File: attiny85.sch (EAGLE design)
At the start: 9 parts, among them U2 ATTINY85V-10SU

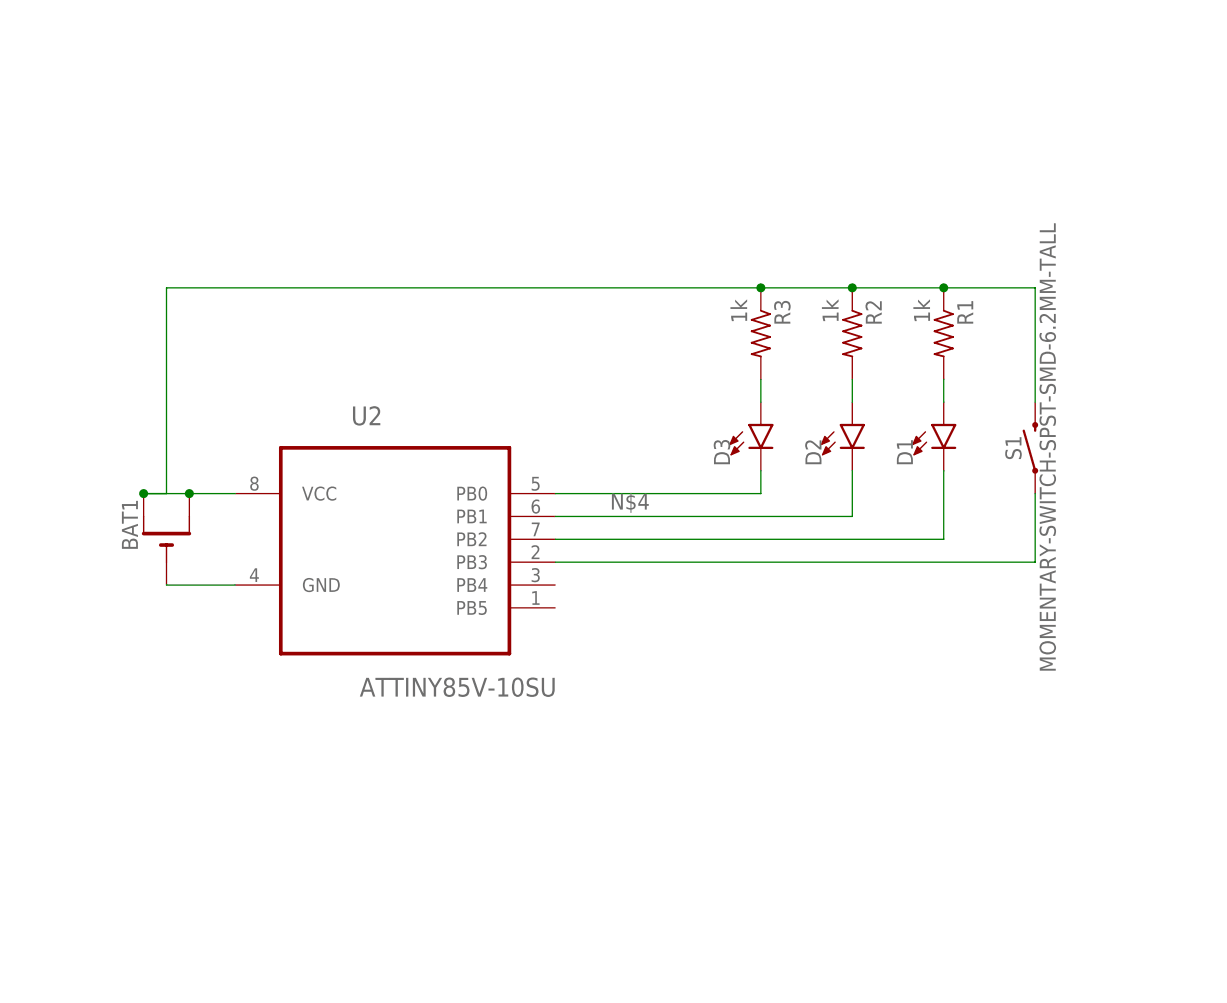
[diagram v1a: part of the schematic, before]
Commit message: Flipping to output through the attiny
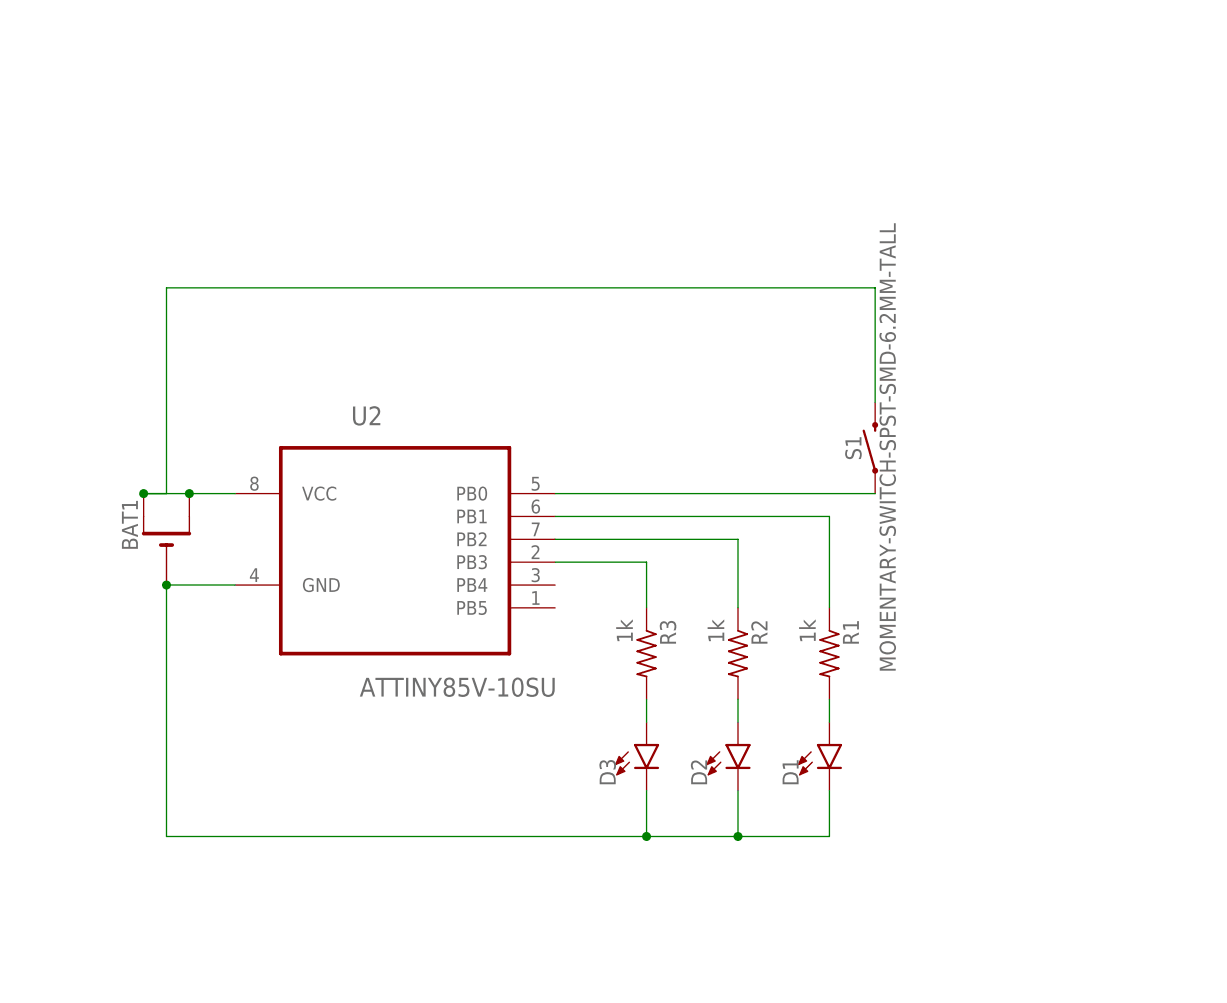
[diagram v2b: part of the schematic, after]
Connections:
- removed net VCC: BAT1.+, BAT1.+1, R1.1, R2.1, R3.1, S1.2, U2.VCC
- new net N$8: R3.1, U2.PB3
- net GND: now also D1.C, D2.C, D3.C
- net N$3: now also BAT1.+, BAT1.+1, S1.2, U2.VCC; no longer D3.C, U2.PB0
- net N$4: now also R1.1; no longer D2.C
- net N$6: now also S1.1, U2.PB0; no longer D1.C, U2.PB2
- net N$7: now also R2.1, U2.PB2; no longer S1.1, U2.PB3
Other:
- moved on the sheet: D1, D2, D3, R1, R2, R3, S1
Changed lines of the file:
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@@
 <instance part="FRAME1" gate="G$1" x="0" y="0"/>
 <instance part="FRAME1" gate="G$2" x="299.72" y="0"/>
-<instance part="R2" gate="G$1" x="106.68" y="220.98" rot="R270"/>
-<instance part="D2" gate="G$1" x="106.68" y="210.82"/>
-<instance part="R3" gate="G$1" x="96.52" y="220.98" rot="R270"/>
-<instance part="D3" gate="G$1" x="96.52" y="210.82"/>
+<instance part="R2" gate="G$1" x="93.98" y="185.42" rot="R270"/>
+<instance part="D2" gate="G$1" x="93.98" y="175.26"/>
+<instance part="R3" gate="G$1" x="83.82" y="185.42" rot="R270"/>
+<instance part="D3" gate="G$1" x="83.82" y="175.26"/>
 <instance part="BAT1" gate="G$1" x="30.48" y="198.12" rot="R90"/>
 <instance part="U2" gate="A" x="55.88" y="200.66"/>
-<instance part="R1" gate="G$1" x="116.84" y="220.98" rot="R270"/>
-<instance part="D1" gate="G$1" x="116.84" y="210.82"/>
-<instance part="S1" gate="G$1" x="127" y="208.28" rot="R90"/>
+<instance part="R1" gate="G$1" x="104.14" y="185.42" rot="R270"/>
+<instance part="D1" gate="G$1" x="104.14" y="175.26"/>
+<instance part="S1" gate="G$1" x="109.22" y="208.28" rot="R90"/>
 </instances>
 <busses>
@@
 <pinref part="R2" gate="G$1" pin="2"/>
 <pinref part="D2" gate="G$1" pin="A"/>
-<wire x1="106.68" y1="215.9" x2="106.68" y2="213.36" width="0.1524" layer="91"/>
+<wire x1="93.98" y1="180.34" x2="93.98" y2="177.8" width="0.1524" layer="91"/>
 </segment>
 </net>
@@
 <pinref part="U2" gate="A" pin="GND"/>
 <wire x1="38.1" y1="193.04" x2="30.48" y2="193.04" width="0.1524" layer="91"/>
-</segment>
-</net>
-<net name="VCC" class="0">
-<segment>
-<pinref part="R2" gate="G$1" pin="1"/>
-<pinref part="BAT1" gate="G$1" pin="+"/>
-<junction x="27.94" y="203.2"/>
-<wire x1="33.02" y1="203.2" x2="27.94" y2="203.2" width="0.1524" layer="91"/>
-<wire x1="27.94" y1="203.2" x2="30.48" y2="203.2" width="0.1524" layer="91"/>
-<wire x1="30.48" y1="203.2" x2="30.48" y2="226.06" width="0.1524" layer="91"/>
-<wire x1="30.48" y1="226.06" x2="96.52" y2="226.06" width="0.1524" layer="91"/>
-<pinref part="BAT1" gate="G$1" pin="+1"/>
-<pinref part="U2" gate="A" pin="VCC"/>
-<wire x1="96.52" y1="226.06" x2="106.68" y2="226.06" width="0.1524" layer="91"/>
-<wire x1="38.1" y1="203.2" x2="33.02" y2="203.2" width="0.1524" layer="91"/>
-<junction x="33.02" y="203.2"/>
-<pinref part="R3" gate="G$1" pin="1"/>
-<junction x="96.52" y="226.06"/>
-<pinref part="R1" gate="G$1" pin="1"/>
-<wire x1="106.68" y1="226.06" x2="116.84" y2="226.06" width="0.1524" layer="91"/>
-<junction x="106.68" y="226.06"/>
-<pinref part="S1" gate="G$1" pin="2"/>
-<wire x1="116.84" y1="226.06" x2="127" y2="226.06" width="0.1524" layer="91"/>
-<wire x1="127" y1="226.06" x2="127" y2="213.36" width="0.1524" layer="91"/>
-<junction x="116.84" y="226.06"/>
+<wire x1="30.48" y1="193.04" x2="30.48" y2="165.1" width="0.1524" layer="91"/>
+<junction x="30.48" y="193.04"/>
+<pinref part="D1" gate="G$1" pin="C"/>
+<wire x1="104.14" y1="170.18" x2="104.14" y2="165.1" width="0.1524" layer="91"/>
+<wire x1="30.48" y1="165.1" x2="83.82" y2="165.1" width="0.1524" layer="91"/>
+<pinref part="D3" gate="G$1" pin="C"/>
+<wire x1="83.82" y1="165.1" x2="93.98" y2="165.1" width="0.1524" layer="91"/>
+<wire x1="93.98" y1="165.1" x2="104.14" y2="165.1" width="0.1524" layer="91"/>
+<wire x1="83.82" y1="170.18" x2="83.82" y2="165.1" width="0.1524" layer="91"/>
+<junction x="83.82" y="165.1"/>
+<pinref part="D2" gate="G$1" pin="C"/>
+<wire x1="93.98" y1="170.18" x2="93.98" y2="165.1" width="0.1524" layer="91"/>
+<junction x="93.98" y="165.1"/>
 </segment>
 </net>
@@
 <pinref part="R3" gate="G$1" pin="2"/>
 <pinref part="D3" gate="G$1" pin="A"/>
-<wire x1="96.52" y1="215.9" x2="96.52" y2="213.36" width="0.1524" layer="91"/>
-</segment>
-</net>
-<net name="N$3" class="0">
-<segment>
-<pinref part="D3" gate="G$1" pin="C"/>
-<pinref part="U2" gate="A" pin="PB0"/>
-<wire x1="96.52" y1="205.74" x2="96.52" y2="203.2" width="0.1524" layer="91"/>
-<wire x1="96.52" y1="203.2" x2="73.66" y2="203.2" width="0.1524" layer="91"/>
-</segment>
-</net>
-<net name="N$4" class="0">
-<segment>
-<wire x1="73.66" y1="200.66" x2="106.68" y2="200.66" width="0.1524" layer="91"/>
-<pinref part="U2" gate="A" pin="PB1"/>
-<label x="79.756" y="201.422" size="1.778" layer="95"/>
-<pinref part="D2" gate="G$1" pin="C"/>
-<wire x1="106.68" y1="205.74" x2="106.68" y2="200.66" width="0.1524" layer="91"/>
+<wire x1="83.82" y1="180.34" x2="83.82" y2="177.8" width="0.1524" layer="91"/>
 </segment>
 </net>
@@
 <pinref part="R1" gate="G$1" pin="2"/>
 <pinref part="D1" gate="G$1" pin="A"/>
-<wire x1="116.84" y1="215.9" x2="116.84" y2="213.36" width="0.1524" layer="91"/>
+<wire x1="104.14" y1="180.34" x2="104.14" y2="177.8" width="0.1524" layer="91"/>
+</segment>
+</net>
+<net name="N$3" class="0">
+<segment>
+<pinref part="BAT1" gate="G$1" pin="+"/>
+<junction x="27.94" y="203.2"/>
+<pinref part="BAT1" gate="G$1" pin="+1"/>
+<pinref part="U2" gate="A" pin="VCC"/>
+<wire x1="38.1" y1="203.2" x2="33.02" y2="203.2" width="0.1524" layer="91"/>
+<junction x="33.02" y="203.2"/>
+<wire x1="33.02" y1="203.2" x2="27.94" y2="203.2" width="0.1524" layer="91"/>
+<wire x1="27.94" y1="203.2" x2="30.48" y2="203.2" width="0.1524" layer="91"/>
+<wire x1="30.48" y1="203.2" x2="30.48" y2="226.06" width="0.1524" layer="91"/>
+<pinref part="S1" gate="G$1" pin="2"/>
+<wire x1="109.22" y1="226.06" x2="109.22" y2="213.36" width="0.1524" layer="91"/>
+<wire x1="30.48" y1="226.06" x2="109.22" y2="226.06" width="0.1524" layer="91"/>
 </segment>
 </net>
 <net name="N$6" class="0">
 <segment>
-<pinref part="D1" gate="G$1" pin="C"/>
-<pinref part="U2" gate="A" pin="PB2"/>
-<wire x1="116.84" y1="205.74" x2="116.84" y2="198.12" width="0.1524" layer="91"/>
-<wire x1="116.84" y1="198.12" x2="73.66" y2="198.12" width="0.1524" layer="91"/>
+<pinref part="U2" gate="A" pin="PB0"/>
+<pinref part="S1" gate="G$1" pin="1"/>
+<wire x1="73.66" y1="203.2" x2="109.22" y2="203.2" width="0.1524" layer="91"/>
+</segment>
+</net>
+<net name="N$4" class="0">
+<segment>
+<pinref part="U2" gate="A" pin="PB1"/>
+<pinref part="R1" gate="G$1" pin="1"/>
+<wire x1="73.66" y1="200.66" x2="104.14" y2="200.66" width="0.1524" layer="91"/>
+<wire x1="104.14" y1="200.66" x2="104.14" y2="190.5" width="0.1524" layer="91"/>
 </segment>
 </net>
 <net name="N$7" class="0">
 <segment>
-<pinref part="S1" gate="G$1" pin="1"/>
-<pinref part="U2" gate="A" pin="PB3"/>
-<wire x1="127" y1="203.2" x2="127" y2="195.58" width="0.1524" layer="91"/>
-<wire x1="127" y1="195.58" x2="73.66" y2="195.58" width="0.1524" layer="91"/>
+<pinref part="U2" gate="A" pin="PB2"/>
+<pinref part="R2" gate="G$1" pin="1"/>
+<wire x1="73.66" y1="198.12" x2="93.98" y2="198.12" width="0.1524" layer="91"/>
+<wire x1="93.98" y1="198.12" x2="93.98" y2="190.5" width="0.1524" layer="91"/>
 </segment>
 </net>
+<net name="N$8" class="0">
+<segment>
+<pinref part="U2" gate="A" pin="PB3"/>
+<pinref part="R3" gate="G$1" pin="1"/>
+<wire x1="73.66" y1="195.58" x2="83.82" y2="195.58" width="0.1524" layer="91"/>
+<wire x1="83.82" y1="195.58" x2="83.82" y2="190.5" width="0.1524" layer="91"/>
+</segment>
+</net>

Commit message: Updating pads and rerouting
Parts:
- BAT1: device adafruit:CR2032SMT -> adafruit-john modded:CR2032SMT
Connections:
- net N$3 renamed VCC
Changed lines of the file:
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@@
 <part name="R3" library="adafruit" deviceset="R-US_" device="M1206" value="1k"/>
 <part name="D3" library="SparkFun-LED" deviceset="LED" device="1206"/>
-<part name="BAT1" library="adafruit" deviceset="CR2032" device="SMT"/>
+<part name="BAT1" library="adafruit-john modded" deviceset="CR2032" device="SMT"/>
 <part name="U2" library="Atmel_By_element14_Batch_1-00" deviceset="ATTINY85V-10SU" device=""/>
 <part name="R1" library="adafruit" deviceset="R-US_" device="M1206" value="1k"/>
@@
 </segment>
 </net>
-<net name="N$3" class="0">
+<net name="VCC" class="0">
 <segment>
 <pinref part="BAT1" gate="G$1" pin="+"/>

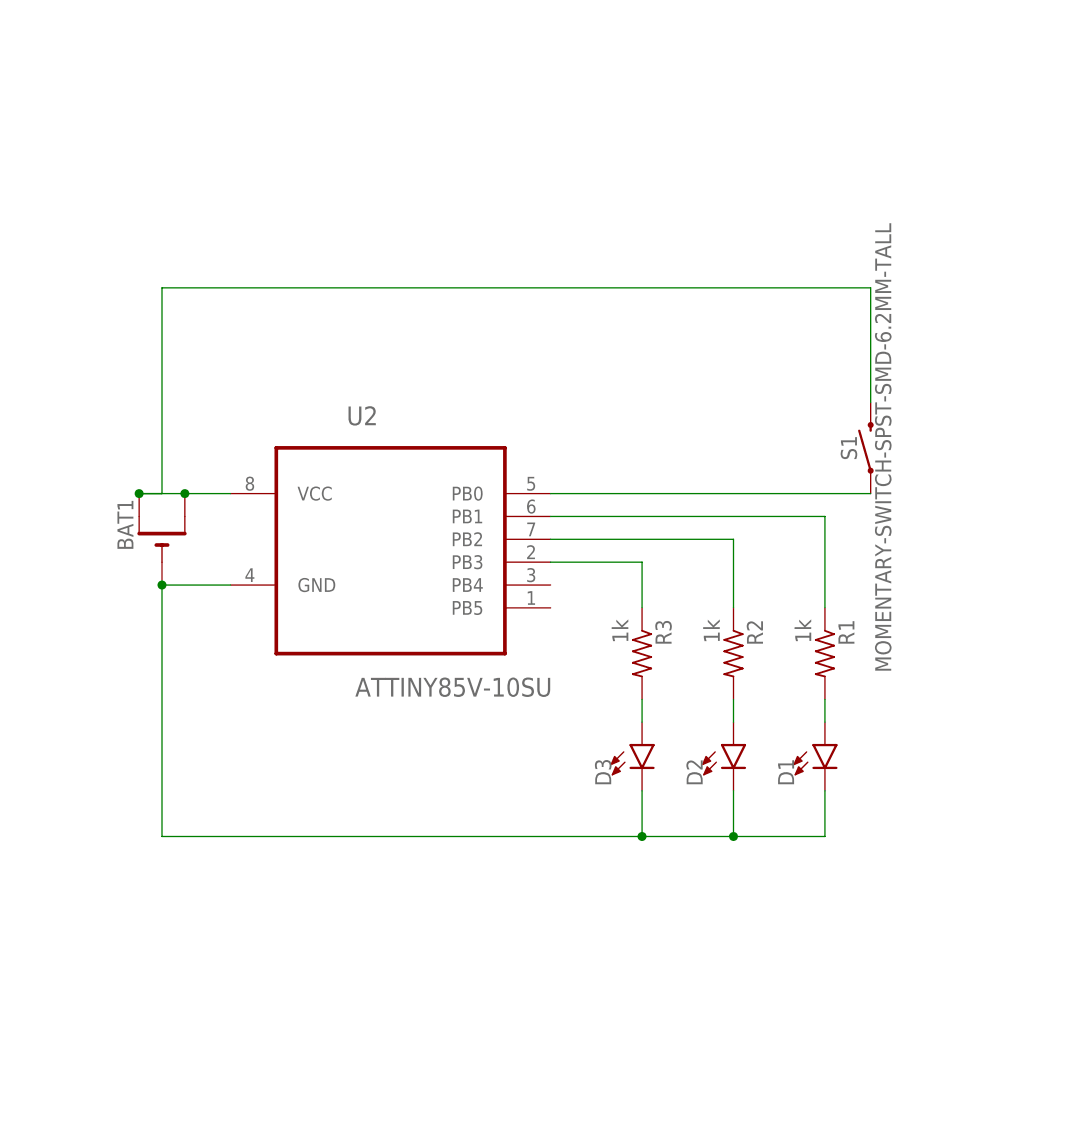
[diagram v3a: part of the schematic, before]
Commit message: Updating the board and schematic
This is a fairly big set of changes based on the prototype, going
to run another round just to be sure since I've got enough time.
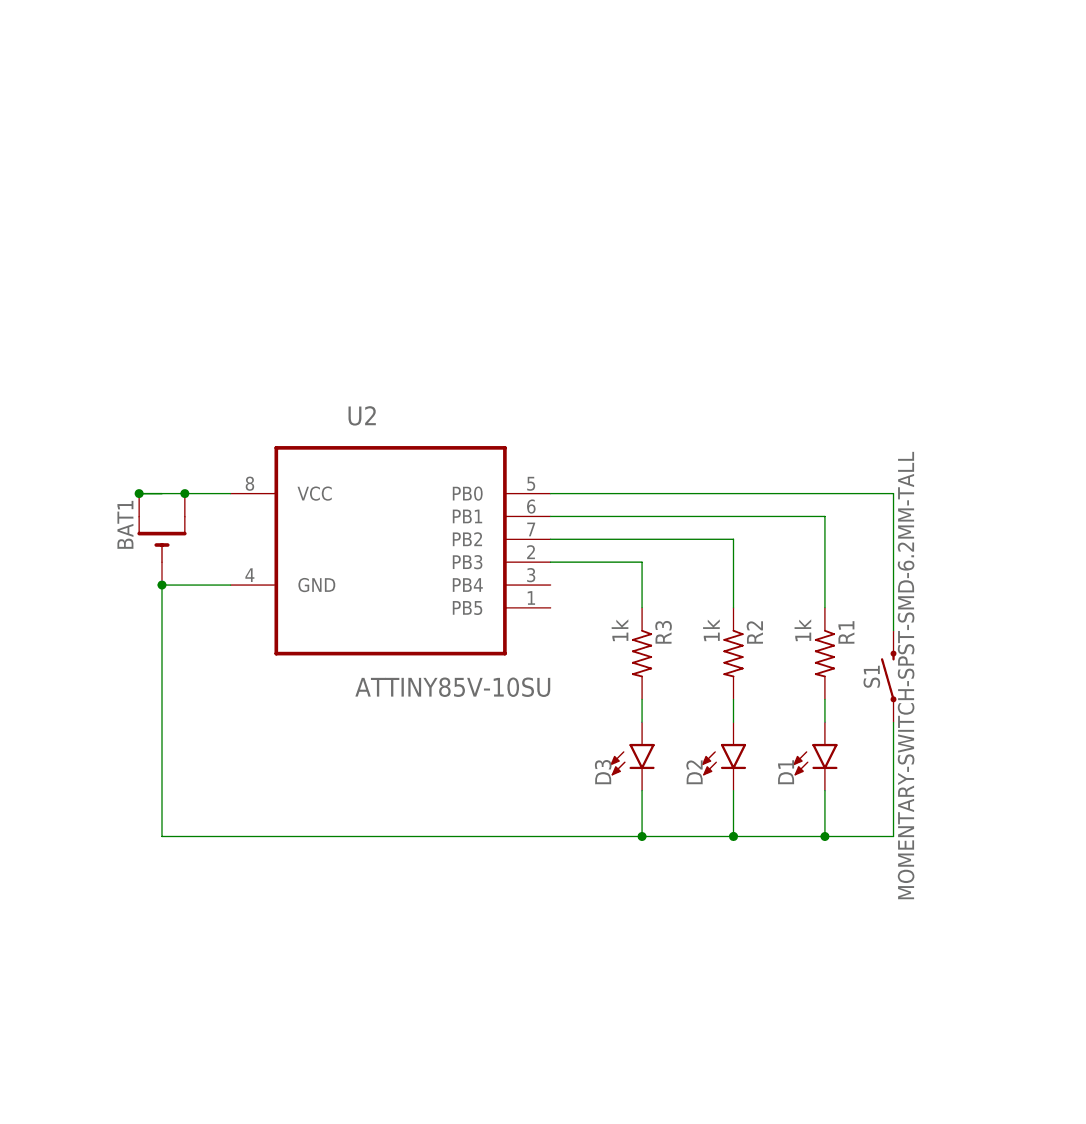
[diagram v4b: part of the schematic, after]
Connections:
- removed net N$6: S1.1, U2.PB0
- new net N$3: S1.2, U2.PB0
- net GND: now also S1.1
- net VCC: no longer S1.2
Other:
- moved on the sheet: S1
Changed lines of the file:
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@@
 <instance part="R1" gate="G$1" x="104.14" y="185.42" rot="R270"/>
 <instance part="D1" gate="G$1" x="104.14" y="175.26"/>
-<instance part="S1" gate="G$1" x="109.22" y="208.28" rot="R90"/>
+<instance part="S1" gate="G$1" x="111.76" y="182.88" rot="R90"/>
 </instances>
 <busses>
@@
 <wire x1="93.98" y1="170.18" x2="93.98" y2="165.1" width="0.1524" layer="91"/>
 <junction x="93.98" y="165.1"/>
+<pinref part="S1" gate="G$1" pin="1"/>
+<wire x1="111.76" y1="177.8" x2="111.76" y2="165.1" width="0.1524" layer="91"/>
+<wire x1="111.76" y1="165.1" x2="104.14" y2="165.1" width="0.1524" layer="91"/>
+<junction x="104.14" y="165.1"/>
 </segment>
 </net>
@@
 <wire x1="33.02" y1="203.2" x2="27.94" y2="203.2" width="0.1524" layer="91"/>
 <wire x1="27.94" y1="203.2" x2="30.48" y2="203.2" width="0.1524" layer="91"/>
-<wire x1="30.48" y1="203.2" x2="30.48" y2="226.06" width="0.1524" layer="91"/>
-<pinref part="S1" gate="G$1" pin="2"/>
-<wire x1="109.22" y1="226.06" x2="109.22" y2="213.36" width="0.1524" layer="91"/>
-<wire x1="30.48" y1="226.06" x2="109.22" y2="226.06" width="0.1524" layer="91"/>
-</segment>
-</net>
-<net name="N$6" class="0">
-<segment>
-<pinref part="U2" gate="A" pin="PB0"/>
-<pinref part="S1" gate="G$1" pin="1"/>
-<wire x1="73.66" y1="203.2" x2="109.22" y2="203.2" width="0.1524" layer="91"/>
 </segment>
 </net>
@@
 </segment>
 </net>
+<net name="N$3" class="0">
+<segment>
+<pinref part="U2" gate="A" pin="PB0"/>
+<pinref part="S1" gate="G$1" pin="2"/>
+<wire x1="73.66" y1="203.2" x2="111.76" y2="203.2" width="0.1524" layer="91"/>
+<wire x1="111.76" y1="203.2" x2="111.76" y2="187.96" width="0.1524" layer="91"/>
+</segment>
+</net>
